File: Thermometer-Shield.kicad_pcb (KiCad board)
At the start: 2 copper layers, 51 parts, among them J1 TempSensor, J10 Out-A, J11 Out-B, J12 Out-C, J13 Out-D, J14 Pin12, J2 Shift-A, J3 Shift-B, J4 Analog, J5 I2C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

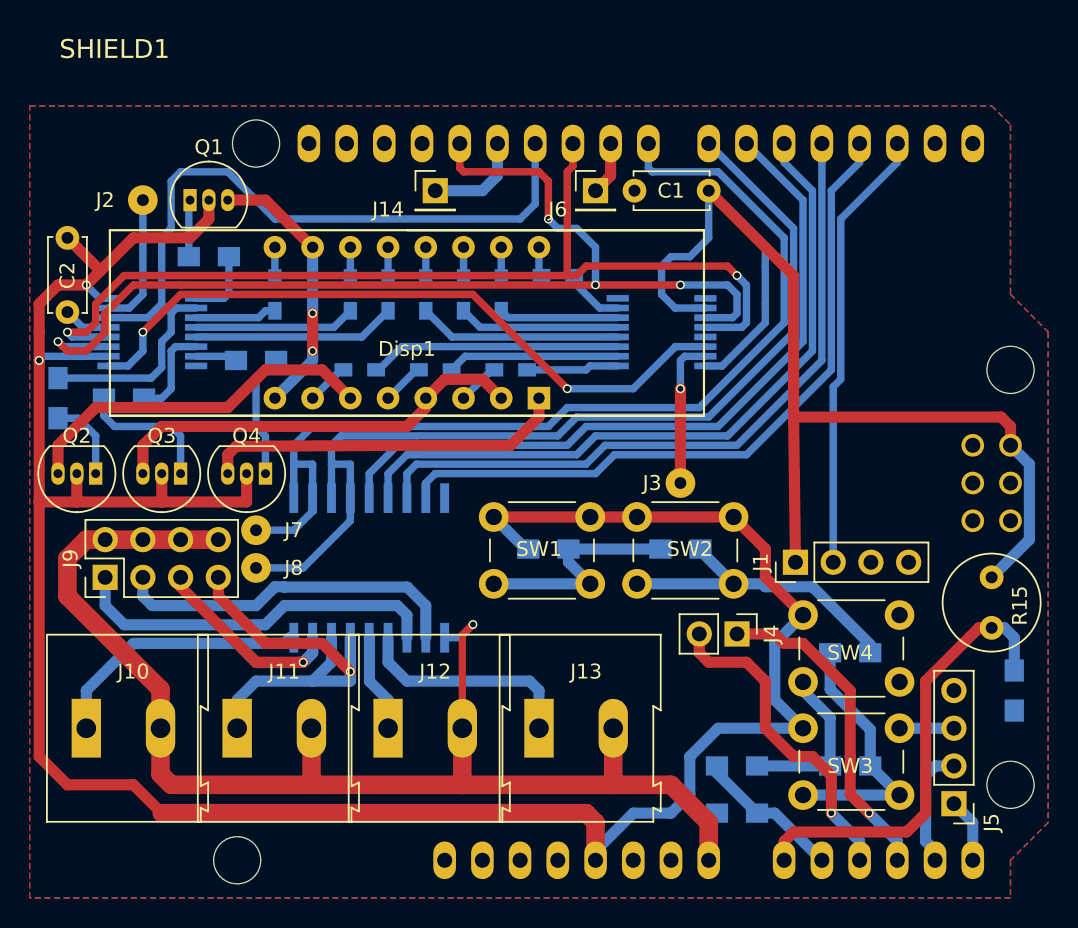
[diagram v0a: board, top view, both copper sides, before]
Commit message: silk screen fixes and additions
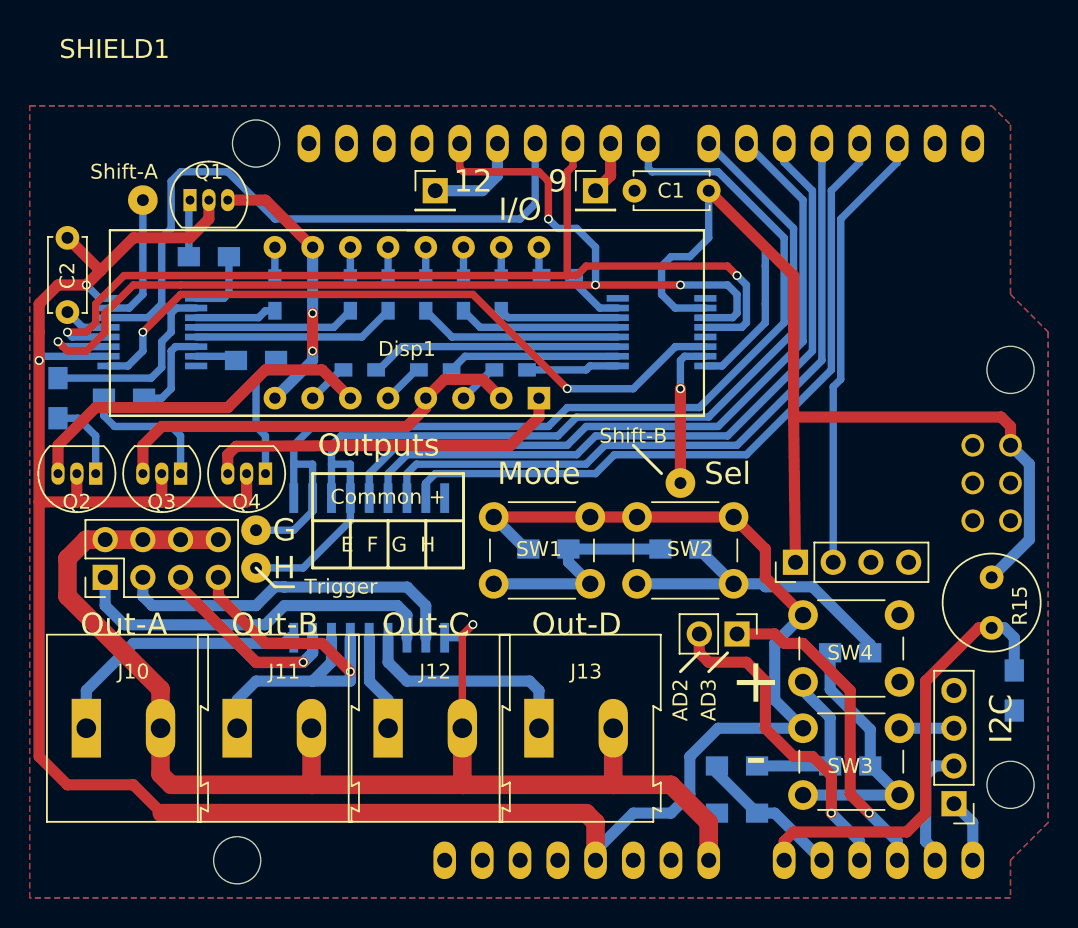
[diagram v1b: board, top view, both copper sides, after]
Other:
- board text added: "+"
- board text added: "-"
- board text added: "12"
- board text added: "9"
- board text added: "AD2"
- board text added: "AD3"
- board text added: "Common + E F G H"
- board text added: "G"
- board text added: "H"
- board text added: "I/O"
- board text added: "I2C"
- board text added: "Mode"
- board text added: "Out-A"
- board text added: "Out-B"
- board text added: "Out-C"
- board text added: "Out-D"
- board text added: "Outputs"
- board text added: "Sel"
- board text added: "Shift-A"
- board text added: "Shift-B"
- board text added: "Trigger"
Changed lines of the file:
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@@
     (links 131)
     (no_connects 5)
-    (area 147.003095 46.5408 218.735 106.16)
+    (area 147.003095 46.5408 218.009 106.16)
     (thickness 1.6)
-    (drawings 0)
+    (drawings 34)
     (tracks 481)
     (zones 0)
@@
     (41 Cmts.User user)
     (42 Eco1.User user)
-    (43 Eco2.User user hide)
-    (44 Edge.Cuts user hide)
+    (43 Eco2.User user)
+    (44 Edge.Cuts user)
     (45 Margin user)
     (46 B.CrtYd user hide)
@@
     (visible_elements FFFE77BF)
     (pcbplotparams
-      (layerselection 0x00000_80000001)
+      (layerselection 0x00030_00000000)
       (usegerberextensions false)
       (excludeedgelayer true)
@@
       (subtractmaskfromsilk false)
       (outputformat 5)
-      (mirror true)
+      (mirror false)
       (drillshape 1)
       (scaleselection 1)
@@
     (descr "TO-92 leads in-line, narrow, oval pads, drill 0.6mm (see NXP sot054_po.pdf)")
     (tags "to-92 sc-43 sc-43a sot54 PA33 transistor")
-    (fp_text reference Q1 (at 1.27 -3.56) (layer F.SilkS)
+    (fp_text reference Q1 (at 1.27 -1.905) (layer F.SilkS)
       (effects (font (size 1 1) (thickness 0.15)))
     )
@@
     (descr "TO-92 leads in-line, narrow, oval pads, drill 0.6mm (see NXP sot054_po.pdf)")
     (tags "to-92 sc-43 sc-43a sot54 PA33 transistor")
-    (fp_text reference Q2 (at 1.27 2.54 180) (layer F.SilkS)
+    (fp_text reference Q2 (at 1.27 -1.905 180) (layer F.SilkS)
       (effects (font (size 1 1) (thickness 0.15)))
     )
@@
     (descr "TO-92 leads in-line, narrow, oval pads, drill 0.6mm (see NXP sot054_po.pdf)")
     (tags "to-92 sc-43 sc-43a sot54 PA33 transistor")
-    (fp_text reference Q3 (at 1.27 2.54 180) (layer F.SilkS)
+    (fp_text reference Q3 (at 1.27 -1.905 180) (layer F.SilkS)
       (effects (font (size 1 1) (thickness 0.15)))
     )
@@
     (descr "TO-92 leads in-line, narrow, oval pads, drill 0.6mm (see NXP sot054_po.pdf)")
     (tags "to-92 sc-43 sc-43a sot54 PA33 transistor")
-    (fp_text reference Q4 (at 1.27 2.54 180) (layer F.SilkS)
+    (fp_text reference Q4 (at 1.27 -1.905 180) (layer F.SilkS)
       (effects (font (size 1 1) (thickness 0.15)))
     )
@@
     (descr "Through hole straight pin header, 1x04, 2.54mm pitch, single row")
     (tags "Through hole pin header THT 1x04 2.54mm single row")
-    (fp_text reference J1 (at 0 -2.33 90) (layer F.SilkS)
+    (fp_text reference J1 (at 0 -2.33 90) (layer F.SilkS) hide
       (effects (font (size 1 1) (thickness 0.15)))
     )
@@
     (descr "Through hole straight pin header, 1x02, 2.54mm pitch, single row")
     (tags "Through hole pin header THT 1x02 2.54mm single row")
-    (fp_text reference J4 (at 0 -2.33 270) (layer F.SilkS)
+    (fp_text reference J4 (at 0 -2.33 270) (layer F.SilkS) hide
       (effects (font (size 1 1) (thickness 0.15)))
     )
@@
     (descr "Through hole straight pin header, 1x04, 2.54mm pitch, single row")
     (tags "Through hole pin header THT 1x04 2.54mm single row")
-    (fp_text reference J5 (at -2.54 -1.27 270) (layer F.SilkS)
+    (fp_text reference J5 (at -2.54 -1.27 270) (layer F.SilkS) hide
       (effects (font (size 1 1) (thickness 0.15)))
     )
@@
     (descr "Through hole straight pin header, 1x01, 2.54mm pitch, single row")
     (tags "Through hole pin header THT 1x01 2.54mm single row")
-    (fp_text reference J6 (at -2.54 1.27) (layer F.SilkS)
+    (fp_text reference J6 (at 0 1.905) (layer F.SilkS) hide
       (effects (font (size 1 1) (thickness 0.15)))
     )
@@
     (descr "Through hole straight pin header, 2x04, 2.54mm pitch, double rows")
     (tags "Through hole pin header THT 2x04 2.54mm double row")
-    (fp_text reference J9 (at 1.27 -2.33 90) (layer F.SilkS)
+    (fp_text reference J9 (at 1.27 -2.33 90) (layer F.SilkS) hide
       (effects (font (size 1 1) (thickness 0.15)))
     )
@@
     (descr "Through hole straight pin header, 1x01, 2.54mm pitch, single row")
     (tags "Through hole pin header THT 1x01 2.54mm single row")
-    (fp_text reference J14 (at -3.175 1.27) (layer F.SilkS)
+    (fp_text reference J14 (at 0 1.905) (layer F.SilkS) hide
       (effects (font (size 1 1) (thickness 0.15)))
     )
@@
   (module Wire_Pads:SolderWirePad_single_0-8mmDrill (layer F.Cu)
     (at 156.21 58.42 90)
-    (fp_text reference J2 (at 0 -2.54 180) (layer F.SilkS)
+    (fp_text reference J2 (at 0 -2.54 180) (layer F.SilkS) hide
       (effects (font (size 1 1) (thickness 0.15)))
     )
@@
   (module Wire_Pads:SolderWirePad_single_0-8mmDrill (layer F.Cu)
     (at 192.405 77.47 270)
-    (fp_text reference J3 (at 0 1.905 360) (layer F.SilkS)
+    (fp_text reference J3 (at 0 1.905 360) (layer F.SilkS) hide
       (effects (font (size 1 1) (thickness 0.15)))
     )
@@
   (module Wire_Pads:SolderWirePad_single_0-8mmDrill (layer F.Cu)
     (at 163.83 80.645)
-    (fp_text reference J7 (at 2.54 0) (layer F.SilkS)
+    (fp_text reference J7 (at 2.54 0) (layer F.SilkS) hide
       (effects (font (size 1 1) (thickness 0.15)))
     )
@@
   (module Wire_Pads:SolderWirePad_single_0-8mmDrill (layer F.Cu)
     (at 163.83 83.185)
-    (fp_text reference J8 (at 2.54 0) (layer F.SilkS)
+    (fp_text reference J8 (at 2.54 0) (layer F.SilkS) hide
       (effects (font (size 1 1) (thickness 0.15)))
     )
@@
     )
   )
+  (gr_text Shift-A (at 154.94 56.515) (layer F.SilkS)
+    (effects (font (size 1 1) (thickness 0.25)))
+  )
+  (gr_text I/O (at 181.61 59.055) (layer F.SilkS)
+    (effects (font (size 1.5 1.5) (thickness 0.3)))
+  )
+  (gr_line (start 165.1 84.455) (end 166.37 84.455) (angle 90) (layer F.SilkS) (width 0.2))
+  (gr_line (start 163.83 83.185) (end 165.1 84.455) (angle 90) (layer F.SilkS) (width 0.2))
+  (gr_text H (at 165.735 83.185) (layer F.SilkS)
+    (effects (font (size 1.5 1.5) (thickness 0.3)))
+  )
+  (gr_text G (at 165.735 80.645) (layer F.SilkS)
+    (effects (font (size 1.5 1.5) (thickness 0.3)))
+  )
+  (gr_text Trigger (at 169.545 84.455) (layer F.SilkS)
+    (effects (font (size 1 1) (thickness 0.25)))
+  )
+  (gr_text Outputs (at 172.085 74.93) (layer F.SilkS)
+    (effects (font (size 1.5 1.5) (thickness 0.3)))
+  )
+  (gr_line (start 175.26 83.185) (end 175.26 80.01) (angle 90) (layer F.SilkS) (width 0.2))
+  (gr_line (start 172.72 80.01) (end 172.72 83.185) (angle 90) (layer F.SilkS) (width 0.2))
+  (gr_line (start 170.18 80.01) (end 170.18 83.185) (angle 90) (layer F.SilkS) (width 0.2))
+  (gr_line (start 177.8 80.01) (end 167.64 80.01) (angle 90) (layer F.SilkS) (width 0.2))
+  (gr_line (start 167.64 83.185) (end 177.8 83.185) (angle 90) (layer F.SilkS) (width 0.2))
+  (gr_line (start 167.64 76.835) (end 167.64 83.185) (angle 90) (layer F.SilkS) (width 0.2))
+  (gr_line (start 177.8 76.835) (end 167.64 76.835) (angle 90) (layer F.SilkS) (width 0.2))
+  (gr_line (start 177.8 83.185) (end 177.8 76.835) (angle 90) (layer F.SilkS) (width 0.2))
+  (gr_text "Common +\n\nE  F  G  H" (at 172.72 80.01) (layer F.SilkS)
+    (effects (font (size 1 1) (thickness 0.25)))
+  )
+  (gr_line (start 191.135 76.835) (end 189.23 74.93) (angle 90) (layer F.SilkS) (width 0.2))
+  (gr_text Shift-B (at 189.23 74.295) (layer F.SilkS)
+    (effects (font (size 1 1) (thickness 0.25)))
+  )
+  (gr_text 9 (at 184.15 57.15) (layer F.SilkS)
+    (effects (font (size 1.5 1.5) (thickness 0.3)))
+  )
+  (gr_text 12 (at 178.435 57.15) (layer F.SilkS)
+    (effects (font (size 1.5 1.5) (thickness 0.3)))
+  )
+  (gr_line (start 192.405 90.17) (end 193.675 88.9) (angle 90) (layer F.SilkS) (width 0.2))
+  (gr_line (start 194.31 90.17) (end 195.58 88.9) (angle 90) (layer F.SilkS) (width 0.2))
+  (gr_text AD3 (at 194.31 92.075 90) (layer F.SilkS)
+    (effects (font (size 1 1) (thickness 0.25)))
+  )
+  (gr_text AD2 (at 192.405 92.075 90) (layer F.SilkS)
+    (effects (font (size 1 1) (thickness 0.25)))
+  )
+  (gr_text I2C (at 213.995 93.345 90) (layer F.SilkS)
+    (effects (font (size 1.5 1.5) (thickness 0.3)))
+  )
+  (gr_text - (at 197.485 95.885) (layer F.SilkS)
+    (effects (font (size 3 3) (thickness 0.3)))
+  )
+  (gr_text + (at 197.485 90.805) (layer F.SilkS)
+    (effects (font (size 3 3) (thickness 0.3)))
+  )
+  (gr_text Sel (at 195.58 76.835) (layer F.SilkS)
+    (effects (font (size 1.5 1.5) (thickness 0.3)))
+  )
+  (gr_text Mode (at 182.88 76.835) (layer F.SilkS)
+    (effects (font (size 1.5 1.5) (thickness 0.3)))
+  )
+  (gr_text "Out-D\n" (at 185.42 86.995) (layer F.SilkS)
+    (effects (font (size 1.5 1.5) (thickness 0.3)))
+  )
+  (gr_text "Out-C\n" (at 175.26 86.995) (layer F.SilkS)
+    (effects (font (size 1.5 1.5) (thickness 0.3)))
+  )
+  (gr_text Out-B (at 165.1 86.995) (layer F.SilkS)
+    (effects (font (size 1.5 1.5) (thickness 0.3)))
+  )
+  (gr_text Out-A (at 154.94 86.995) (layer F.SilkS)
+    (effects (font (size 1.5 1.5) (thickness 0.3)))
+  )
   (segment (start 161.925 76.835) (end 161.925 75.565) (width 0.75) (layer F.Cu) (net 1))
